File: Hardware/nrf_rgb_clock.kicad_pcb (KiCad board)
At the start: 2 copper layers, 230 x 230 mm, 190 parts, among them U1 NRF54L15-CAAA-Rx

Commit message: progressed layout
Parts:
- added 3V3: TestPoint, TestPoint:TestPoint_THTPad_2.0x2.0mm_Drill1.0mm, F.Cu at (164.0, 154.2)
- added AE1: 2450AT43A100E, ProjectFootprints:2450AT43A100E, F.Cu at (150.3, 128.1)
- added C1: 10u, Capacitor_SMD:C_0805_2012Metric, F.Cu at (161.3, 134.4)
- added C10: 4u7 100VDC, Capacitor_SMD:C_1206_3216Metric, F.Cu at (161.2, 165.7)
- added C11: 4u7 100VDC, Capacitor_SMD:C_1206_3216Metric, F.Cu at (163.7, 165.7)
- added C12: 100n 100VDC, Capacitor_SMD:C_0805_2012Metric, F.Cu at (171.4, 166.2)
- added C13: 22u 6.3V, Capacitor_SMD:C_0805_2012Metric, F.Cu at (164.9, 158.9)
- added C14: 22u 6.3V, Capacitor_SMD:C_0805_2012Metric, F.Cu at (164.9, 156.9)
- added C15: 15p, Capacitor_SMD:C_0805_2012Metric, F.Cu at (165.9, 161.7)
- added C16: 22n, Capacitor_SMD:C_0805_2012Metric, F.Cu at (171.2, 160.2)
- added C17: ?p, Capacitor_SMD:C_0201_0603Metric, F.Cu at (152.8, 127.5)
- added C18: ?p, Capacitor_SMD:C_0201_0603Metric, F.Cu at (158.0, 127.7)
- added D174: ACDBMS2100-HF, Diode_SMD:D_SOD-123F, F.Cu at (171.4, 170.2)
- added FB1: 120R@100Mhz, Resistor_SMD:R_0402_1005Metric, F.Cu at (160.6, 128.3)
- added GND: TestPoint, TestPoint:TestPoint_THTPad_2.0x2.0mm_Drill1.0mm, F.Cu at (160.7, 154.2)
- added J1: Conn_01x02, ProjectFootprints:SHDR4W113P700X508_2X2_1039X1200X1200P, F.Cu at (147.5, 167.2)
- added L5: 10u, ProjectFootprints:NRS5040T3R3NMGJV, F.Cu at (176.4, 167.7)
- added R1: 0R, Resistor_SMD:R_0805_2012Metric, F.Cu at (165.9, 166.2)
- added R2: 210k, Resistor_SMD:R_0805_2012Metric, F.Cu at (163.9, 161.7)
- added R3: 68k, Resistor_SMD:R_0805_2012Metric, F.Cu at (159.9, 161.7)
- added R4: 47k, Resistor_SMD:R_0805_2012Metric, F.Cu at (161.9, 161.7)
- added U2: MP4562, ProjectFootprints:MP4562, F.Cu at (168.7, 163.9)
- added Y1: 32MHz, Crystal:Crystal_SMD_3225-4Pin_3.2x2.5mm, F.Cu at (155.4, 127.5)
- C2, C3: footprint Capacitor_SMD:C_0201_0603Metric -> Capacitor_SMD:C_0402_1005Metric
- C4, C5: value 2u2 -> 2u2 50V; footprint Capacitor_SMD:C_0201_0603Metric -> Capacitor_SMD:C_0603_1608Metric
- C6: value 10n -> 10n 50V
- C7: value 3p9 -> 3p9 50V
- C8, C9: value 1p2 -> 1p2 50V
- D1, D10, D100, D101, D102, D103, D104, D105, D106, D107, D108, D109, D11, D110, D111, D112, D113, D114, D115, D116, D117, D118, D119, D12, D120, D121, D122, D123, D124, D125, D126, D127, D128, D129, D13, D130, D131, D132, D133, D134, D135, D136, D137, D138, D139, D14, D140, D141, D142, D143, D144, D145, D146, D147, D148, D149, D15, D150, D151, D152, D153, D154, D155, D156, D157, D158, D159, D16, D160, D161, D162, D163, D164, D165, D166, D167, D168, D169, D17, D170, D171, D172, D173, D18, D19, D2, D20, D21, D22, D23, D24, D25, D26, D27, D28, D29, D3, D30, D31, D32, D33, D34, D35, D36, D37, D38, D39, D4, D40, D41, D42, D43, D44, D45, D46, D47, D48, D49, D5, D50, D51, D52, D53, D54, D55, D56, D57, D58, D59, D6, D60, D61, D62, D63, D64, D65, D66, D67, D68, D69, D7, D70, D71, D72, D73, D74, D75, D76, D77, D78, D79, D8, D80, D81, D82, D83, D84, D85, D86, D87, D88, D89, D9, D90, D91, D92, D93, D94, D95, D96, D97, D98, D99: value ~ -> WS2813b
- L1: footprint LED_SMD:LED_0402_1005Metric -> LED_SMD:LED_0201_0603Metric
- L2: footprint Inductor_SMD:L_0201_0603Metric -> LED_SMD:LED_0201_0603Metric
- moved L2 174.0 mm to (152.3, 131.4), turned to 180 degrees
- moved L3 172.0 mm to (154.5, 131.4), turned to 180 degrees
- moved C8 170.9 mm to (153.4, 131.8), turned to 90 degrees
- moved L4 170.1 mm to (156.6, 131.4), turned to 180 degrees
- moved C9 169.0 mm to (155.6, 131.8), turned to 90 degrees
- moved L1 166.0 mm to (161.4, 129.2), turned to 180 degrees
- moved C7 165.6 mm to (159.2, 127.1), turned to -90 degrees
- moved C6 164.5 mm to (160.0, 127.1), turned to -90 degrees
- moved C5 163.1 mm to (158.8, 133.9), turned to 90 degrees
- moved U1 162.9 mm to (160.7, 130.9)
- moved C4 160.8 mm to (161.9, 127.1), turned to 180 degrees
- moved C2 160.4 mm to (160.8, 132.9), turned to 180 degrees
- moved C3 158.8 mm to (162.8, 132.2), turned to 90 degrees
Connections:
- D1 pad 4: /led_circle/LED_DI -> LED_CIRCLE
- D1 pad 6: /led_circle/LED_BI -> LED_CIRCLE
- D60 pad 4: /led_segment/LED_DI -> LED_SEGMENTS
- D60 pad 6: /led_segment/LED_BI -> LED_SEGMENTS
- U1 pad B4: unconnected-(U1-P1.13-PadB4) -> LED_CIRCLE
- U1 pad B5: unconnected-(U1-P1.14-PadB5) -> LED_SEGMENTS
- U1 pad C5: NRF_XC_OPT1 -> unconnected-(U1-P1.00-PadC5)
- U1 pad C6: NRF_XC_OPT2 -> unconnected-(U1-P1.01-PadC6)
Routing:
- net +3V3: track 0.00 -> 29.8 mm
- net V_EXT: track 0.00 -> 22.4 mm
- net GND: track 86.7 -> 100.2 mm, vias 170 -> 200
- net Net-(U1-DECA): track 0.00 -> 11.9 mm, vias 0 -> 3
- net NRF_XC2: track 0.00 -> 10.3 mm
- net NRF_XC1: track 0.00 -> 10.3 mm
- net Net-(U2-FB): track 0.00 -> 9.14 mm
- net VDD_NRF: track 0.00 -> 8.93 mm
- net Net-(D174-K): track 0.00 -> 8.89 mm
- net Net-(U2-FREQ): track 0.00 -> 7.88 mm
- net Net-(U2-SS): track 0.00 -> 2.91 mm
- net Net-(U1-DECD): track 0.00 -> 2.71 mm
- net NRF_ANT: track 0.00 -> 2.64 mm
- net NRF_RF: track 0.00 -> 2.42 mm
- net Net-(U2-EN): track 0.00 -> 1.79 mm
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
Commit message: layout progress
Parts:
- removed U1: NRF54L15-CAAA-Rx, ProjectFootprints:WLCSP 300
- added C19: 100n, Capacitor_SMD:C_0402_1005Metric, B.Cu at (238.9, 153.1)
- added C20: 100n, Capacitor_SMD:C_0402_1005Metric, B.Cu at (230.9, 154.3)
- added J3: Conn_01x07_Pin, Connector_PinHeader_2.54mm:PinHeader_1x07_P2.54mm_Vertical, F.Cu at (241.7, 161.5)
- added U4: ~, ProjectFootprints:QFN-48_EP_6x6_Pitch0.4mm, B.Cu at (234.9, 152.2)
- 3V3, AE1, C1, C10, C11, C12, C13, C14, C15, C16, C17, C18, C2, C3, C4, C5, C6, C7, C8, C9, D174, FB1, GND, J1, L1, L2, L3, L4, L5, R1, R2, R3, R4, U2, Y1: moved to B.Cu
- moved J1 96.6 mm to (236.8, 130.3)
- moved AE1 87.6 mm to (230.4, 163.5), turned to 180 degrees
- moved L2 87.4 mm to (234.5, 161.0), turned to -90 degrees
- moved C8 85.5 mm to (234.2, 159.9), turned to 0 degrees
- moved L3 84.6 mm to (234.5, 158.8), turned to -90 degrees
- moved C17 83.5 mm to (229.6, 160.4), turned to 0 degrees
- moved C9 82.8 mm to (234.2, 157.7), turned to 0 degrees
- moved L4 81.9 mm to (234.5, 156.7), turned to -90 degrees
- moved D174 80.1 mm to (241.4, 131.1), turned to 90 degrees
- moved Y1 80.1 mm to (229.7, 157.8), turned to 90 degrees
- moved C18 76.6 mm to (229.5, 155.2), turned to 180 degrees
- moved C12 76.6 mm to (241.4, 135.1), turned to 90 degrees
- moved R1 76.6 mm to (235.9, 135.1), turned to 90 degrees
- moved C10 76.2 mm to (231.1, 135.6), turned to -90 degrees
- moved C11 76.2 mm to (233.6, 135.6), turned to -90 degrees
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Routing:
- net LED_CIRCLE: track 0.00 -> 155.0 mm, vias 0 -> 2
- net LED_SEGMENTS: track 0.00 -> 89.2 mm, vias 0 -> 2
- net VDD_NRF: track 8.93 -> 31.9 mm, vias 0 -> 3
- net +3V3: track 29.8 -> 48.4 mm
- net GND: track 100.2 -> 111.7 mm, vias 200 -> 236
- net NRF_SWDIO: track 0.00 -> 8.22 mm
- net NRF_NRST: track 0.00 -> 7.33 mm
- net NRF_SWDCLK: track 0.00 -> 6.85 mm
- net Net-(D174-K): track 8.89 -> 11.0 mm
- net V_EXT: track 22.4 -> 20.7 mm
- net NRF_ANT: track 2.64 -> 1.46 mm
- net Net-(U4-DECA): track 11.9 -> 13.0 mm, vias 3 -> 2
- net NRF_RF: track 2.42 -> 3.46 mm
- net NRF_XC2: track 10.3 -> 11.2 mm
- net NRF_XC1: track 10.3 -> 11.0 mm
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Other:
- board text added: "LED_CIRCLE"
- board text added: "LED_SEGMENTS"
- board text added: "NRST"
- board text added: "SWDCLK"
- board text added: "SWDIO"

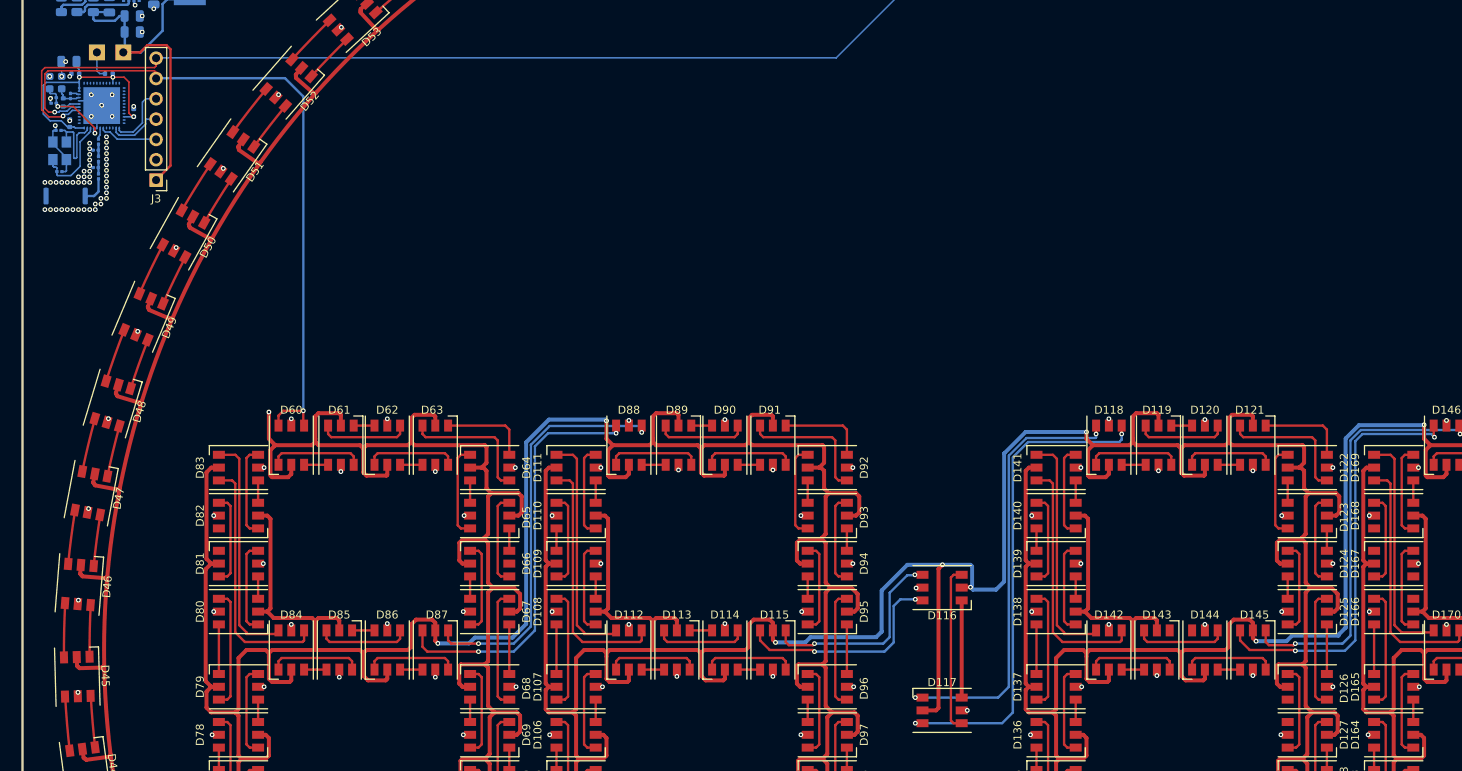
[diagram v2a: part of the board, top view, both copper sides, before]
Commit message: impedance match 50R + 4 layer
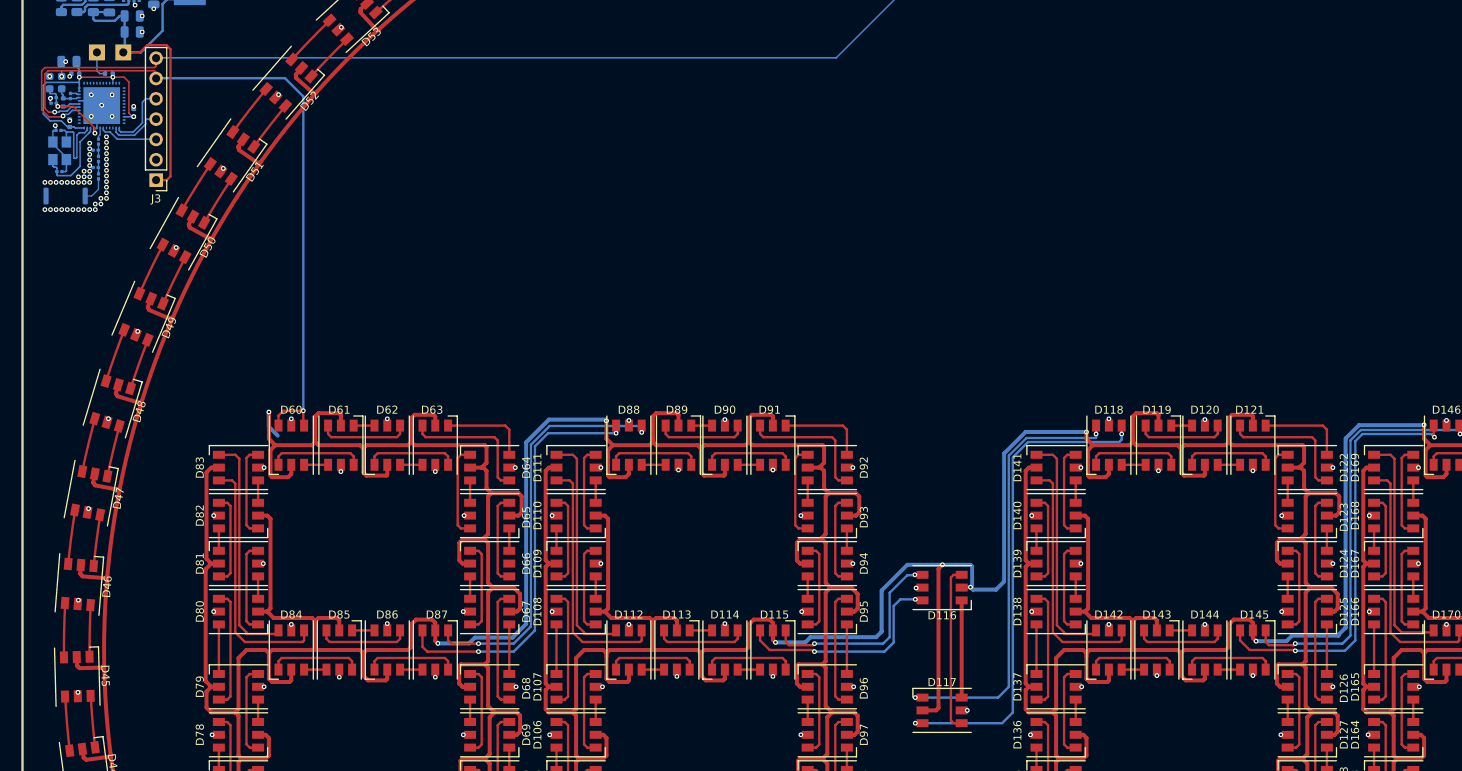
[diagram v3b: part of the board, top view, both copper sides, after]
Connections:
- D10 pad 4: Net-(D10-BI) -> Net-(D10-DI)
- D9 pad 3: Net-(D10-BI) -> Net-(D10-DI)
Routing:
- net +5V: track 1999.6 -> 2003.1 mm
- net Net-(D81-BO): track 0.00 -> 2.80 mm
- net Net-(D167-BO): track 0.00 -> 2.80 mm
- net Net-(D166-DO): track 0.00 -> 2.80 mm
- net Net-(D143-BO): track 0.00 -> 2.80 mm
- net Net-(D126-DO): track 0.00 -> 2.80 mm
- net +3V3: track 48.4 -> 49.2 mm
- added copper zone on In2.Cu, net +5V
- added copper zone on In1.Cu, net GND
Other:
- copper layers 2 -> 4
- board text added: "3V3"
- board text added: "GND"
